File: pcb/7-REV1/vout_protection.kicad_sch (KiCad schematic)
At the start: 37 parts, among them J1 Conn_01x10, J2 Conn_01x09, Q3 AO6802, Q6 MMBT7002K, U16 AP2127, U17 LM393

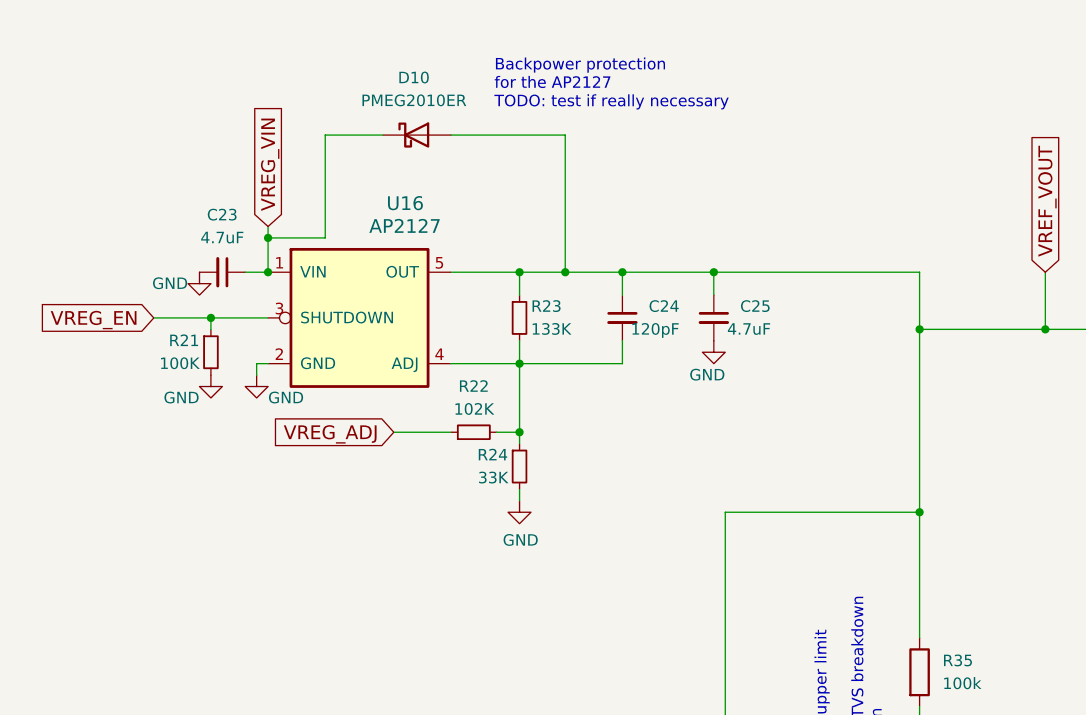
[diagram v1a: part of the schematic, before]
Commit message: adapt protection for the AP2127 voltage regulator
- add a PMEG2020EJ for backflow-handling
- remove the previous backflow protection circuit
- remove the AP2127+circuit from the "VOUT protection" sheet, it was redundant
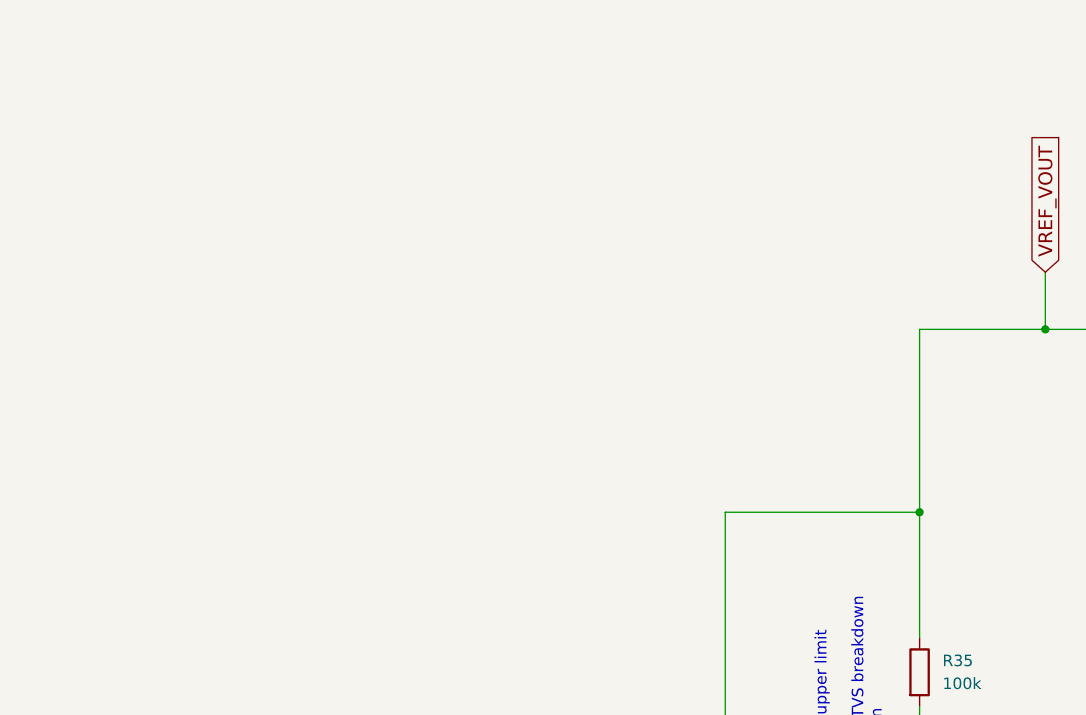
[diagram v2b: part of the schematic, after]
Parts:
- removed C23, C25: 4.7uF, Capacitor_SMD:C_0402_1005Metric, symbol Device:C_Small
- removed C24: 120pF, Capacitor_SMD:C_0402_1005Metric, symbol Device:C_Small
- removed D10: PMEG2010ER, symbol Device:D_Schottky
- removed R21: 100K, Resistor_SMD:R_0402_1005Metric, symbol Device:R_Small
- removed R22: 102K, Resistor_SMD:R_0402_1005Metric, symbol Device:R_Small
- removed R23: 133K, Resistor_SMD:R_0402_1005Metric, symbol Device:R_Small
- removed R24: 33K, Resistor_SMD:R_0402_1005Metric, symbol Device:R_Small
- removed U16: AP2127, Package_TO_SOT_SMD:SOT-23-5, symbol dp-vreg:MCP1824
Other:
- note removed: "Backpower protection for the AP2127 TODO: test if really necessary"

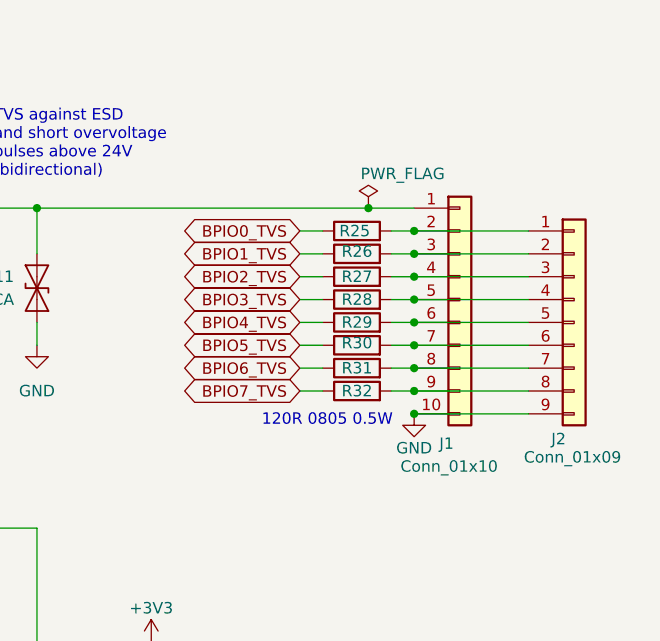
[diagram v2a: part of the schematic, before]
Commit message: adapt the IO-port protection
- move to the bpu-iobuffer sheet, remove duplicate on VOUT-protection
- use SP3002-04JTG in SOT363 instead of the larger IP4220CZ6F
- add datasheet, resistor wattage to part fields
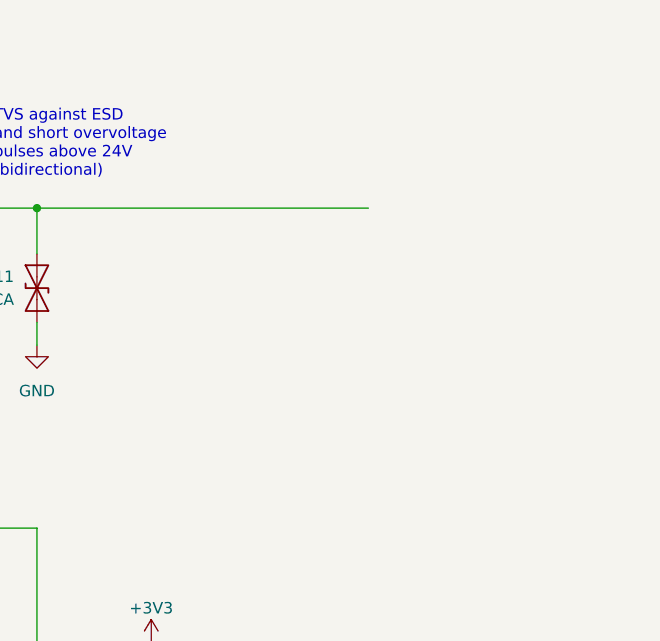
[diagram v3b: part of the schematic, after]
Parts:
- removed J1: Conn_01x10, Connector_PinHeader_2.54mm:PinHeader_1x10_P2.54mm_Vertical, symbol Connector_Generic:Conn_01x10
- removed J2: Conn_01x09, Connector_JST:JST_SH_SM09B-SRSS-TB_1x09-1MP_P1.00mm_Horizontal, symbol Connector_Generic:Conn_01x09
- removed R25, R26, R27, R28, R29, R30, R31, R32: 120R, Resistor_SMD:R_0805_2012Metric_Pad1.20x1.40mm_HandSolder, symbol Device:R
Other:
- note removed: "120R 0805 0.5W"

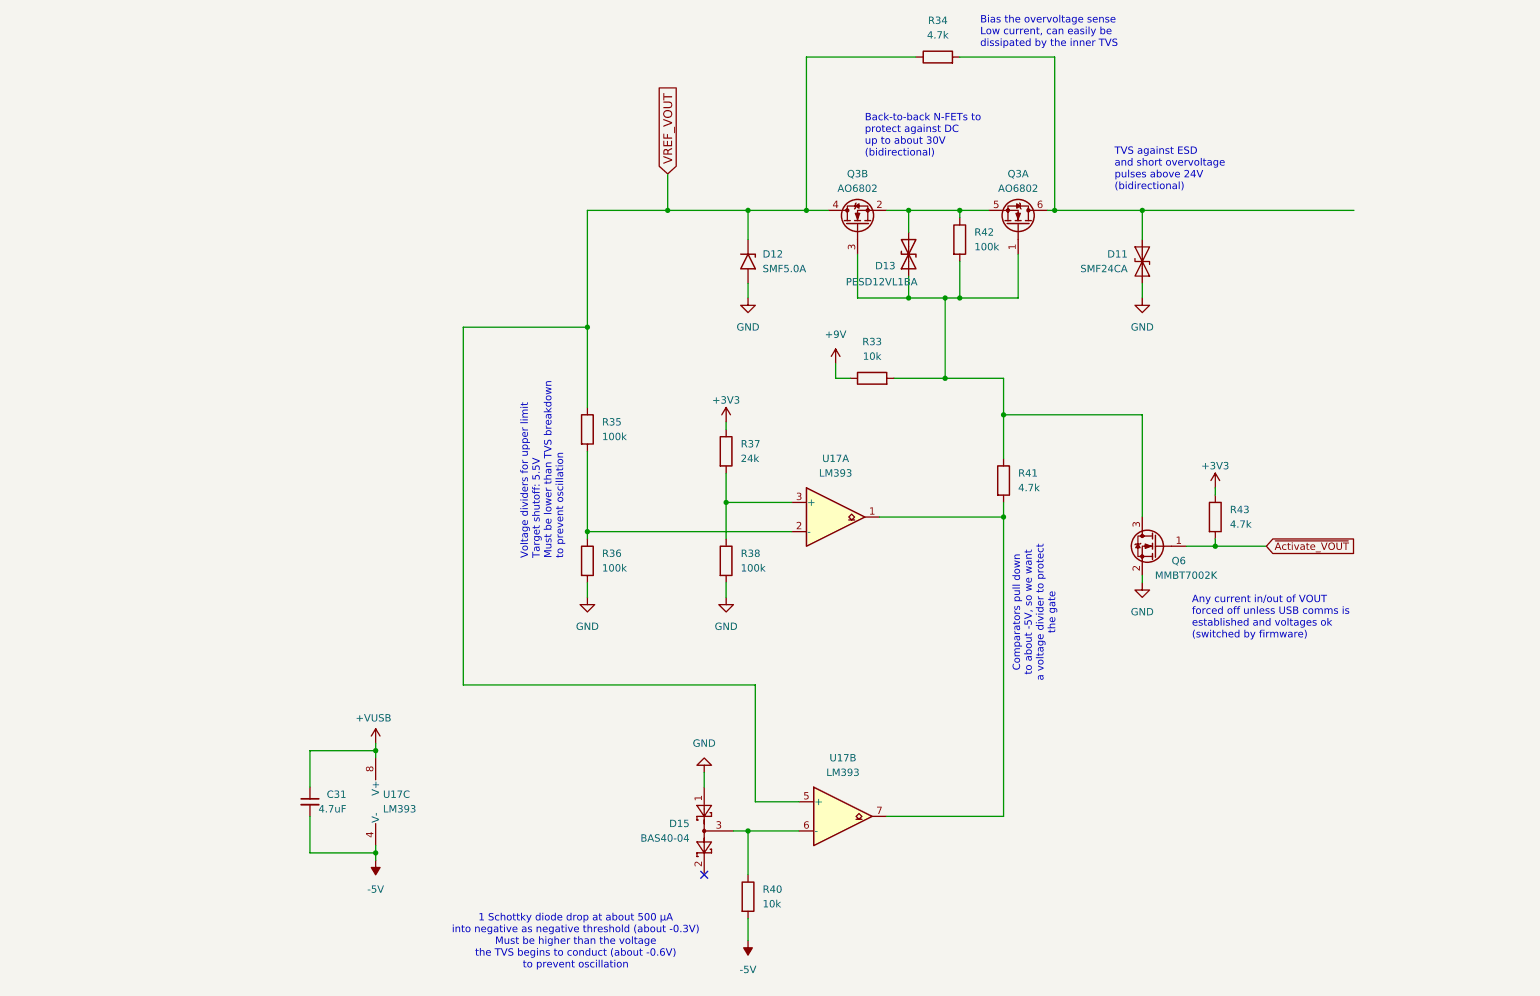
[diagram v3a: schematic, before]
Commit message: adapt VOUT protection as tested
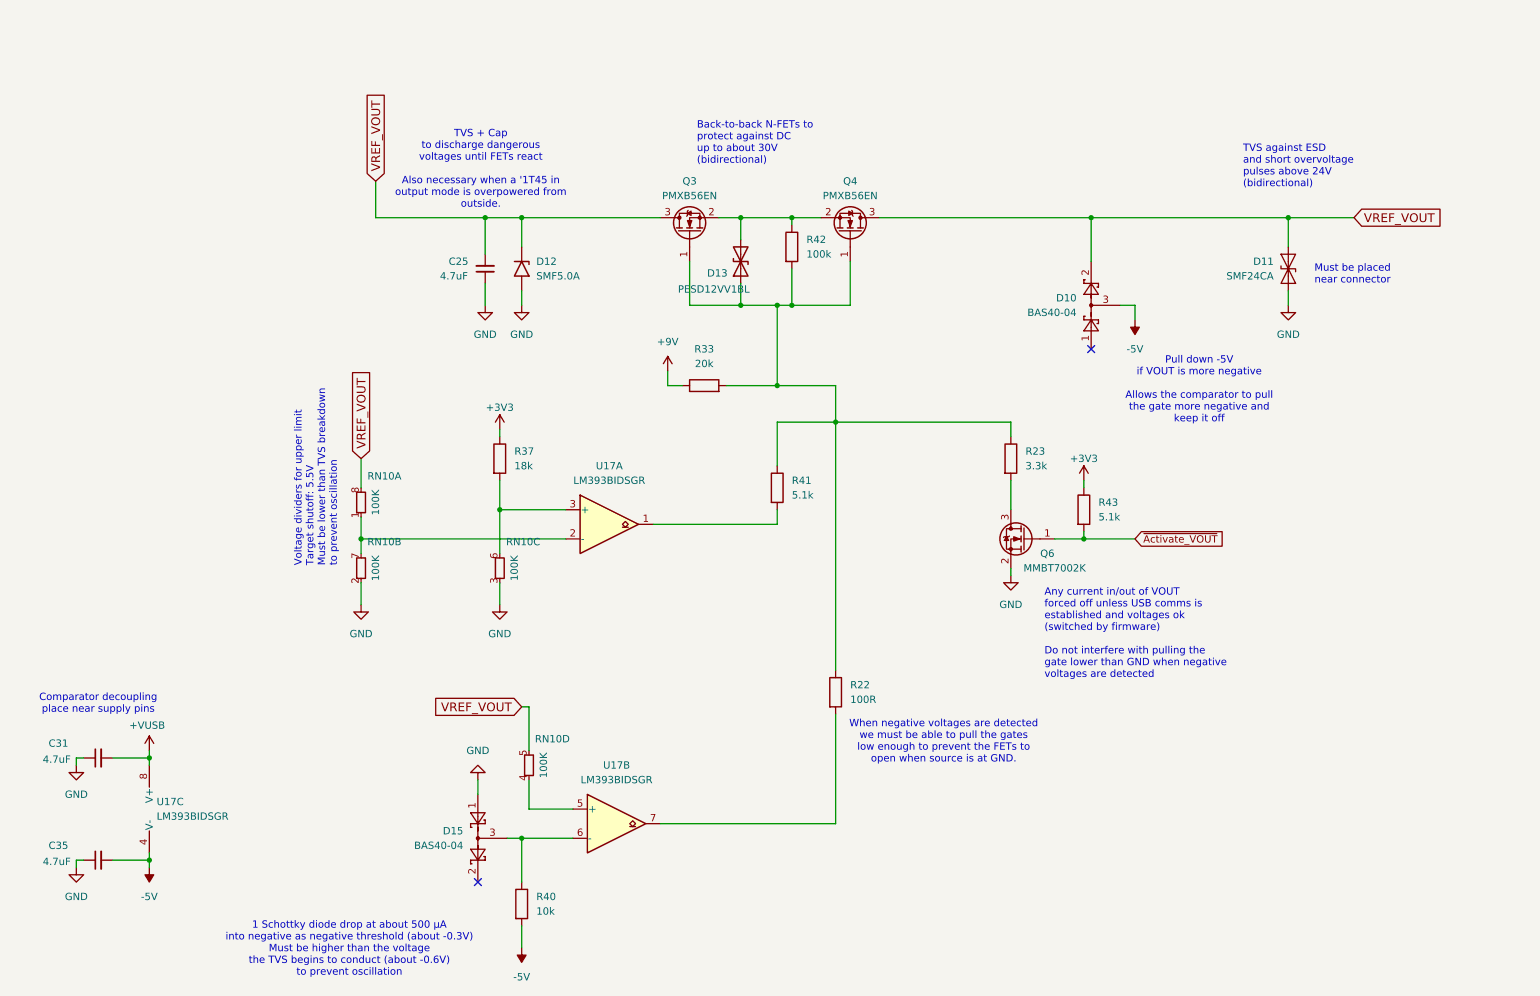
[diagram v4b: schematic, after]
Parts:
- removed Q3: AO6802, symbol Device:Q_Dual_NMOS_G1S2G2D2S1D1
- removed R34: 4.7k, symbol Device:R
- removed R35, R36, R38: 100k, symbol Device:R
- added C25, C35: 4.7uF, Capacitor_SMD:C_0402_1005Metric, symbol Device:C_Small
- added D10: BAS40-04, Package_TO_SOT_SMD:SOT-523, symbol Diode:BAS40-04
- added Q3, Q4: PMXB56EN, modules:DFN1010D-3_SOT1215_NEX, symbol Device:Q_NMOS_GSD
- added R22: 100R, Resistor_SMD:R_0402_1005Metric, symbol Device:R
- added R23: 3.3k, Resistor_SMD:R_0402_1005Metric, symbol Device:R
- added RN10: 100K, Resistor_SMD:R_Array_Convex_4x0402, symbol dp-rarray:R_Array
- D11, D12: footprint (none) -> Diode_SMD:D_SMF
- D13: value PESD12VL1BA -> PESD12VV1BL; footprint (none) -> Diode_SMD:D_SOD-882D
- R33: value 10k -> 20k; footprint (none) -> Resistor_SMD:R_0402_1005Metric
- R37: value 24k -> 18k; footprint (none) -> Resistor_SMD:R_0402_1005Metric
- R40, R42: footprint (none) -> Resistor_SMD:R_0402_1005Metric
- R41, R43: value 4.7k -> 5.1k; footprint (none) -> Resistor_SMD:R_0402_1005Metric
- U17: value LM393 -> LM393BIDSGR; footprint (none) -> Package_SON:WSON-8-1EP_2x2mm_P0.5mm_EP0.9x1.6mm
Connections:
- net +VUSB: now also C31.2; no longer C31.1
- net -5V: now also C35.2, D10.3; no longer C31.2
- net GND: now also C31.1, C25.1, C35.1, RN10.2 (R1.1), RN10.3 (R1.1)
- net VREF_VOUT: now also D11.2 (A2), C25.2, D10.2, Q3.3 (D), Q4.3 (D), RN10.5 (R1.8), RN10.8 (R1.8); no longer U17.5 (+)
- net at R37.2, U17.3 (+): now also RN10.6 (R1.8)
- net at R41.2, U17.1: no longer U17.7
- net at U17.2 (-): now also RN10.1 (R1.1), RN10.7 (R1.8)
- net at D13.1 (A1), R33.2, R41.1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: now also Q3.1 (G), Q4.1 (G), R22.1, R23.1; no longer Q6.3 (D)
- net at D13.2 (A2), R42.1: now also Q3.2 (S), Q4.2 (S)
- new net: Q6.3 (D), R23.2
- new net: RN10.4 (R1.1), U17.5 (+)
- new net: R22.2, U17.7
- no-connect marks 1 -> 2
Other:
- note added: "Any current in/out of VOUT forced off unless USB comms is established and voltages ok (switched by firmware) Do not interfere with pulling the gate lower than GND when negative voltages are detected"
- note added: "Comparator decoupling place near supply pins"
- note added: "Must be placed near connector"
- note added: "Pull down -5V if VOUT is more negative Allows the comparator to pull the gate more negative and keep it off"
- note added: "TVS + Cap to discharge dangerous voltages until FETs react Also necessary when a '1T45 in output mode is overpowered from outside."
- note added: "When negative voltages are detected we must be able to pull the gates low enough to prevent the FETs to open when source is at GND."
- note removed: "Any current in/out of VOUT forced off unless USB comms is established and voltages ok (switched by firmware)"
- note removed: "Bias the overvoltage sense Low current, can easily be dissipated by the inner TVS"
- note removed: "Comparators pull down to about -5V, so we want a voltage divider to protect the gate"
- moved on the sheet: C31, D11, D12, D15, Q6, R33, R37, R40, R41, R42, R43, U17A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

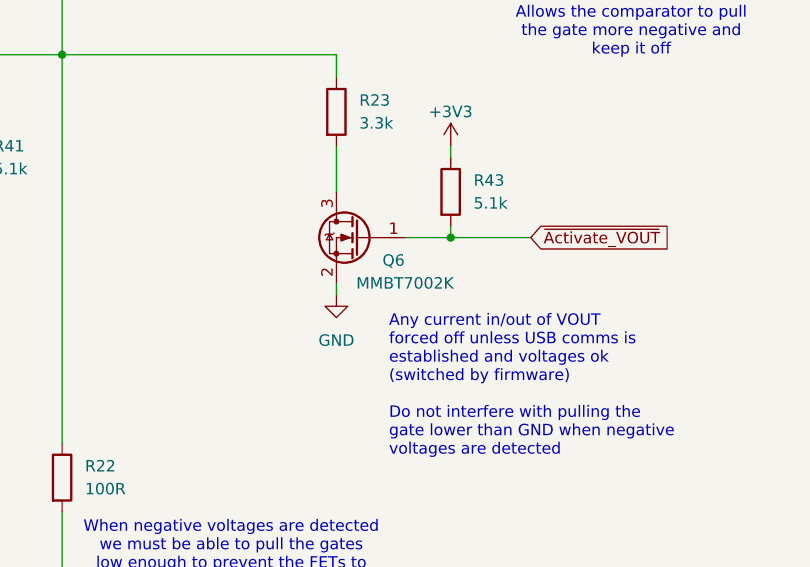
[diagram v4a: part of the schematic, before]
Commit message: replace MMBT7002K in SOT-23 with 2N7002T in SOT-523
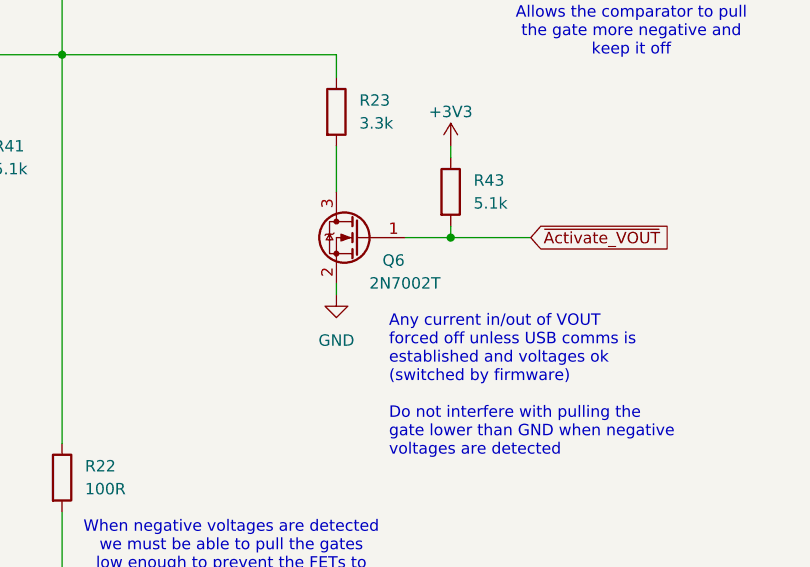
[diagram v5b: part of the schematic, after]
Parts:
- Q6: value MMBT7002K -> 2N7002T; footprint Package_TO_SOT_SMD:SOT-23 -> Package_TO_SOT_SMD:SOT-523
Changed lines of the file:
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@@
 			)
 		)
-		(property "Value" "MMBT7002K"
+		(property "Value" "2N7002T"
 			(at 198.12 109.22 0)
 			(effects
@@
 			)
 		)
-		(property "Footprint" "Package_TO_SOT_SMD:SOT-23"
+		(property "Footprint" "Package_TO_SOT_SMD:SOT-523"
 			(at 187.96 106.045 0)
 			(effects
@@
 			)
 		)
-		(property "Datasheet" "https://www.fairchildsemi.com/datasheets/BS/BSS138.pdf"
+		(property "Datasheet" "https://www.onsemi.com/download/data-sheet/pdf/2n7002t-d.pdf"
 			(at 193.04 104.14 0)
 			(effects

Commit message: add DFN1010D-3 / SOT1215 footprint for PMXB56EN mosfets
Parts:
- Q3, Q4: footprint modules:DFN1010D-3_SOT1215_NEX -> DFN1010D-3:DFN1010D-3_SOT1215_NEX
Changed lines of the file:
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@@
 			)
 		)
-		(property "Footprint" "modules:DFN1010D-3_SOT1215_NEX"
+		(property "Footprint" "DFN1010D-3:DFN1010D-3_SOT1215_NEX"
 			(at 132.08 45.72 0)
 			(effects
@@
 			)
 		)
-		(property "Footprint" "modules:DFN1010D-3_SOT1215_NEX"
+		(property "Footprint" "DFN1010D-3:DFN1010D-3_SOT1215_NEX"
 			(at 165.1 45.72 0)
 			(effects
